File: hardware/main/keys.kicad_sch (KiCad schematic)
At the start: 86 parts, among them SW1 Esc, SW10 a, SW11 \, SW12 Fn, SW13 F2, SW14 2, SW15 w, SW16 s, SW17 z, SW18 Tux, SW19 F3, SW2 F1, SW20 3, SW21 e, SW22 d, SW23 c, SW24 Alt, SW25 F4, SW26 4, SW27 r, SW28 f, SW29 v, SW3 tilde, SW31 F5, SW32 5, SW33 t, SW34 g, SW35 b, SW36 F6, SW37 6, SW38 y, SW39 h, SW4 Tab, SW40 n, SW41 F7, SW42 7, SW43 u, SW44 j, SW45 m, SW46 Space, SW47 F8, SW48 8, SW49 i, SW5 Caps Lock, SW50 k, SW51 ,, SW52 F9, SW53 9, SW54 o, SW55 l, SW56 ., SW57 F10, SW58 0, SW59 p, SW6 Shift, SW60 ;, SW61 /, SW62 Alt Gr, SW63 F11, SW64 -, SW65 [, SW66 ', SW67 Menu, SW68 F12, SW69 =, SW7 Ctrl, SW70 ], SW71 \, SW72 Shift, SW73 Ctrl, SW74 Print, SW75 Backspace, SW76 Enter, SW77 Left, SW78 Scroll Lock, SW79 Up, SW8 1, SW80 Down, SW81 Pause, SW82 INS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

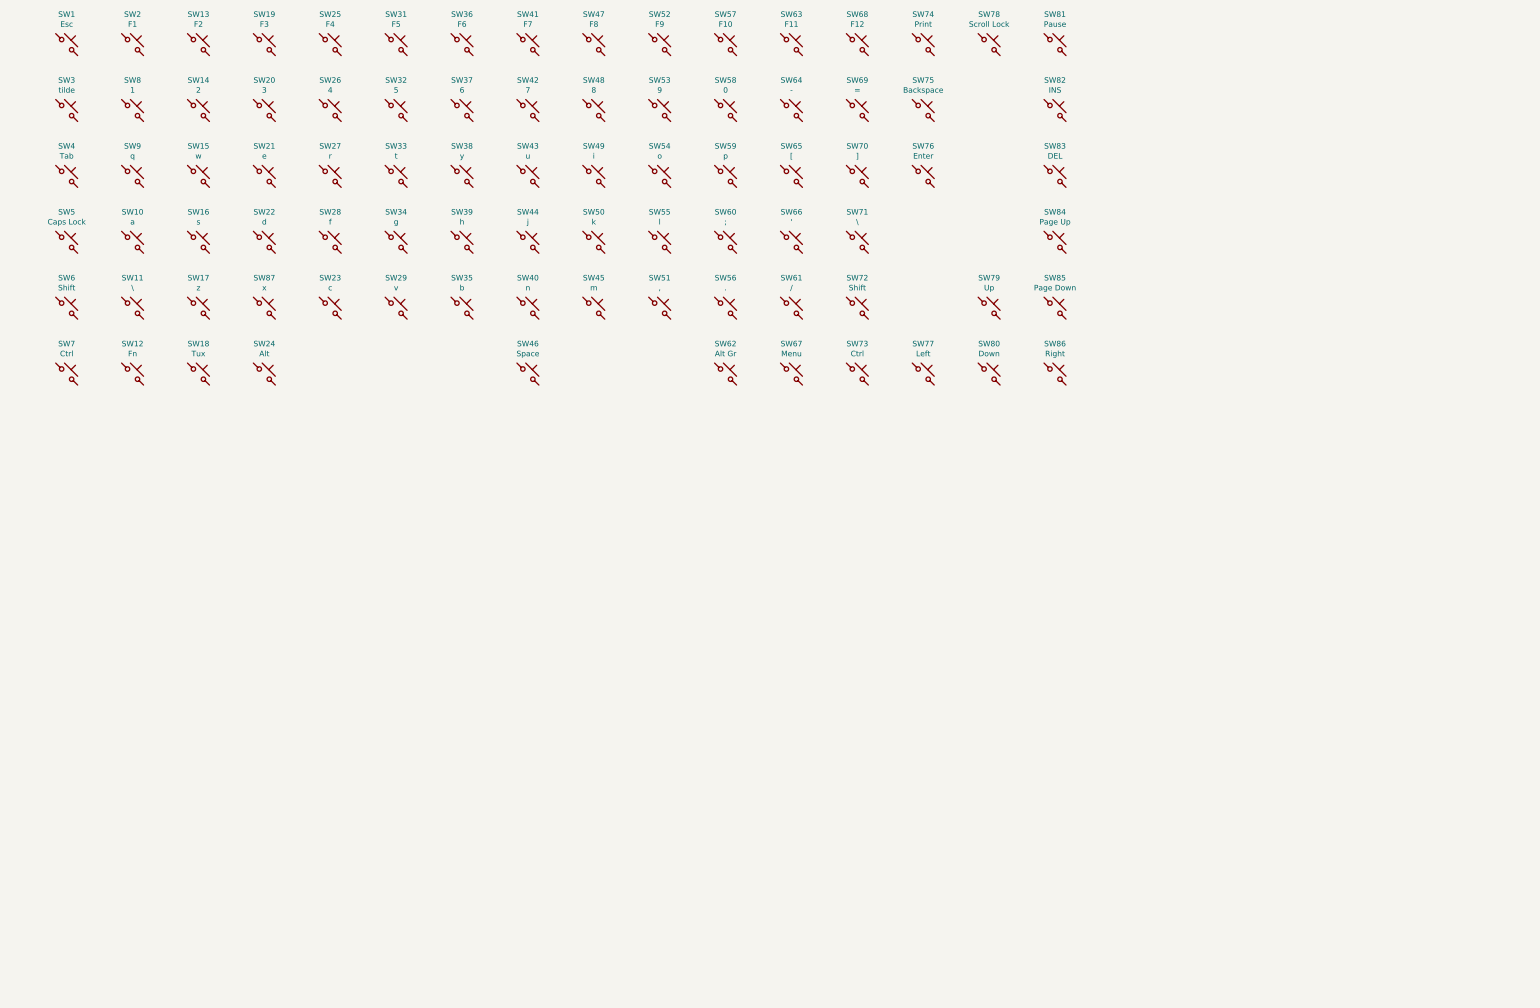
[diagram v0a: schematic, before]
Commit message: Implement the key matrix on the PCB
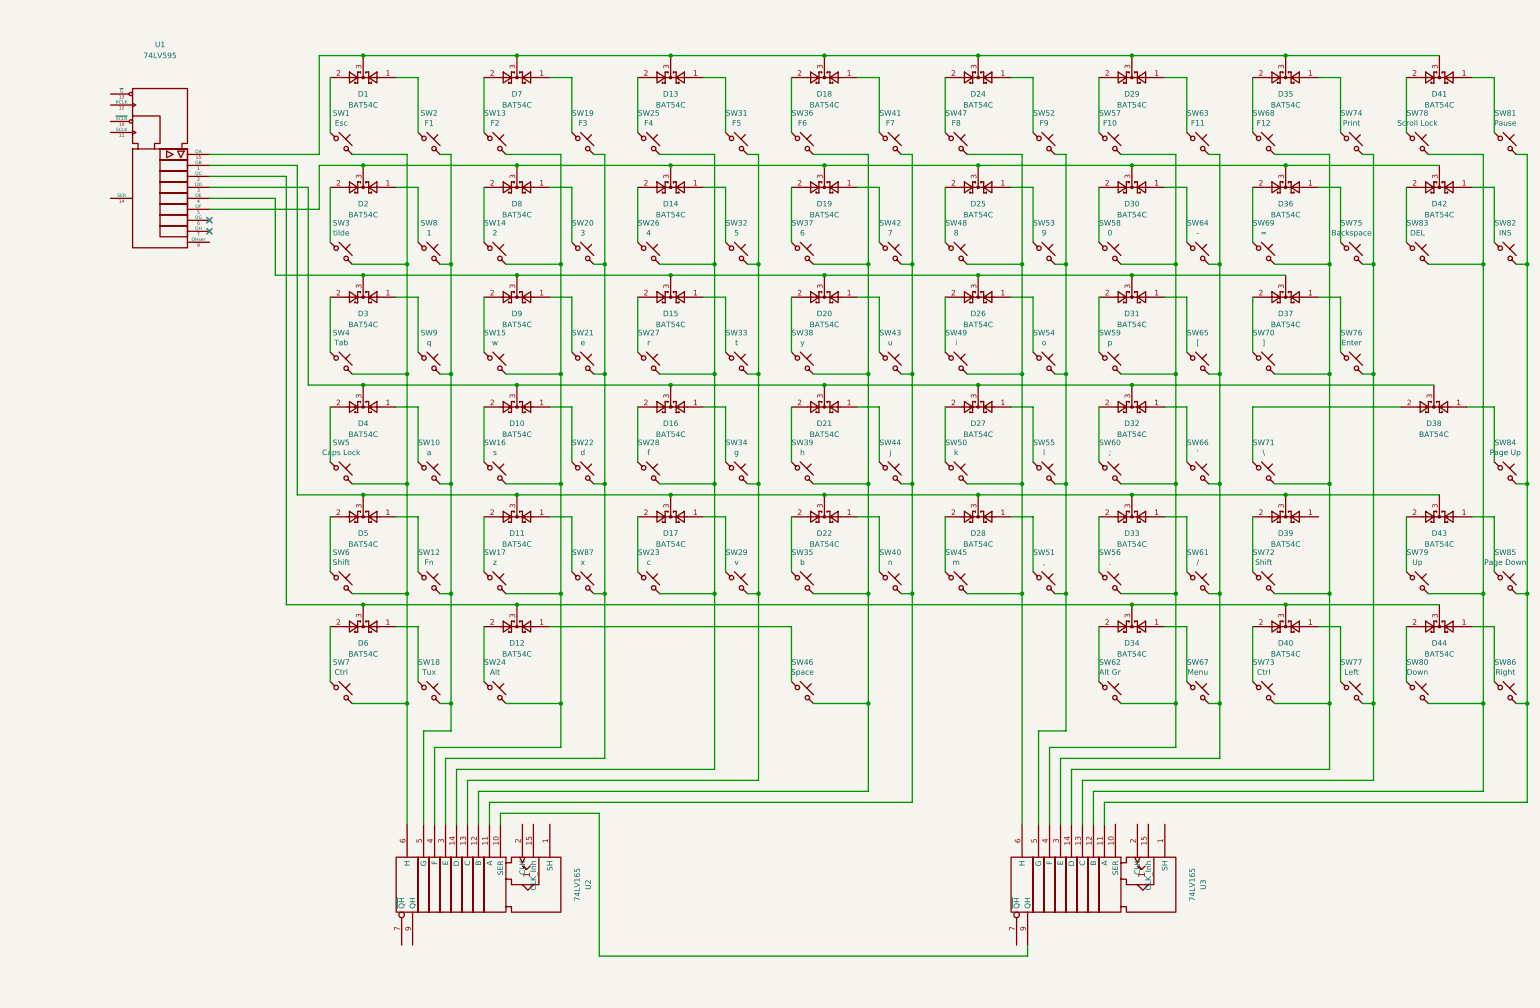
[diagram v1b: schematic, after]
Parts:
- removed SW11: \, footprints:SW_Cherry_MX_1.00u_PCB, symbol Switch:SW_Push_45deg
- added D1, D10, D11, D12, D13, D14, D15, D16, D17, D18, D19, D2, D20, D21, D22, D24, D25, D26, D27, D28, D29, D3, D30, D31, D32, D33, D34, D35, D36, D37, D38, D39, D4, D40, D41, D42, D43, D44, D5, D6, D7, D8, D9: BAT54C, Package_TO_SOT_SMD:SOT-23, symbol Diode:BAT54C
- added U1: 74LV595, Package_SO:TSSOP-16_4.4x5mm_P0.65mm, symbol 74xx_IEEE:74LS595
- added U2, U3: 74LV165, Package_SO:TSSOP-16_4.4x5mm_P0.65mm, symbol 74xx_IEEE:74165
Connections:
- net at SW5.1: now also D4.2
- net at SW5.2: now also SW1.2, SW3.2, SW4.2, SW6.2, SW7.2, U2.6 (H)
- net at SW9.1: now also D3.1
- net at SW9.2: now also SW10.2, SW12.2, SW18.2, SW2.2, SW8.2, U2.5 (G)
- net at SW44.1: now also D21.1
- net at SW44.2: now also SW40.2, SW41.2, SW42.2, SW43.2, U2.11 (A)
- net at SW84.1: now also D38.1
- net at SW84.2: now also SW81.2, SW82.2, SW85.2, SW86.2, U3.11 (A)
- net at SW6.1: now also D5.2
- net at SW65.1: now also D31.1
- net at SW65.2: now also SW61.2, SW63.2, SW64.2, SW66.2, SW67.2, U3.3 (E)
- net at SW56.1: now also D33.2
- net at SW56.2: now also SW57.2, SW58.2, SW59.2, SW60.2, SW62.2, U3.4 (F)
- net at SW78.1: now also D41.2
- net at SW78.2: now also SW79.2, SW80.2, SW83.2, U3.12 (B)
- net at SW73.1: now also D40.2
- net at SW73.2: now also SW68.2, SW69.2, SW70.2, SW71.2, SW72.2, U3.14 (D)
- net at SW7.1: now also D6.2
- net at SW87.1: now also D11.1
- net at SW87.2: now also SW19.2, SW20.2, SW21.2, SW22.2, U2.3 (E)
- net at SW17.1: now also D11.2
- net at SW17.2: now also SW13.2, SW14.2, SW15.2, SW16.2, SW24.2, U2.4 (F)
- net at SW72.1: now also D39.2
- net at SW63.1: now also D29.1
- net at SW50.1: now also D27.2
- net at SW50.2: now also SW45.2, SW47.2, SW48.2, SW49.2, U3.6 (H)
- net at SW8.1: now also D2.1
- net at SW39.1: now also D21.2
- net at SW39.2: now also SW35.2, SW36.2, SW37.2, SW38.2, SW46.2, U2.12 (B)
- net at SW60.1: now also D32.2
- net at SW51.1: now also D28.1
- net at SW51.2: now also SW52.2, SW53.2, SW54.2, SW55.2, U3.5 (G)
- net at SW32.1: now also D14.1
- net at SW32.2: now also SW29.2, SW31.2, SW33.2, SW34.2, U2.13 (C)
- net at SW66.1: now also D32.1
- net at SW20.1: now also D8.1
- net at SW25.1: now also D13.2
- net at SW25.2: now also SW23.2, SW26.2, SW27.2, SW28.2, U2.14 (D)
- net at SW86.1: now also D44.1
- net at SW2.1: now also D1.1
- net at SW81.1: now also D41.1
- net at SW41.1: now also D18.1
- net at SW85.1: now also D43.1
- net at SW27.1: now also D15.2
- net at SW3.1: now also D2.2
- net at SW22.1: now also D10.1
- net at SW48.1: now also D25.2
- net at SW21.1: now also D9.1
- net at SW58.1: now also D30.2
- net at SW37.1: now also D19.2
- net at SW82.1: now also D42.1
- net at SW42.1: now also D19.1
- net at SW53.1: now also D25.1
- net at SW69.1: now also D36.2
- net at SW26.1: now also D14.2
- net at SW16.1: now also D10.2
- net at SW70.1: now also D37.2
- net at SW23.1: now also D17.2
- net at SW57.1: now also D29.2
- net at SW47.1: now also D24.2
- net at SW46.1: now also D12.1
- net at SW80.1: now also D44.2
- net at SW79.1: now also D43.2
- net at SW62.1: now also D34.2
- net at SW64.1: now also D30.1
- net at SW55.1: now also D27.1
- net at SW13.1: now also D7.2
- net at SW35.1: now also D22.2
- net at SW59.1: now also D31.2
- net at SW49.1: now also D26.2
- net at SW54.1: now also D26.1
- net at SW67.1: now also D34.1
- net at SW74.1: now also D35.1
- net at SW74.2: now also SW75.2, SW76.2, SW77.2, U3.13 (C)
- net at SW24.1: now also D12.2
- net at SW1.1: now also D1.2
- net at SW83.1: now also D42.2
- net at SW33.1: now also D15.1
- net at SW77.1: now also D40.1
- net at SW14.1: now also D8.2
- net at SW10.1: now also D4.1
- net at SW18.1: now also D6.1
- net at SW43.1: now also D20.1
- net at SW12.1: now also D5.1
- net at SW4.1: now also D3.2
- net at SW75.1: now also D36.1
- net at SW40.1: now also D22.1
- net at SW15.1: now also D9.2
- net at SW71.1: now also D38.2
- net at SW31.1: now also D13.1
- net at SW19.1: now also D7.1
- net at SW76.1: now also D37.1
- net at SW29.1: now also D17.1
- net at SW36.1: now also D18.2
- net at SW38.1: now also D20.2
- net at SW52.1: now also D24.1
- net at SW45.1: now also D28.2
- net at SW28.1: now also D16.2
- net at SW34.1: now also D16.1
- net at SW68.1: now also D35.2
- net at SW61.1: now also D33.1
- new net: D11.3, D17.3, D22.3, D28.3, D33.3, D39.3, D43.3, D5.3, U1.1 (QB)
- new net: D1.3, D13.3, D18.3, D24.3, D29.3, D35.3, D41.3, D7.3, U1.15 (QA)
- new net: D12.3, D34.3, D40.3, D44.3, D6.3, U1.2 (QC)
- new net: D14.3, D19.3, D2.3, D25.3, D30.3, D36.3, D42.3, D8.3, U1.5 (QF)
- new net: D10.3, D16.3, D21.3, D27.3, D32.3, D38.3, D4.3, U1.3 (QD)
- new net: U2.10 (SER), U3.9 (QH)
- new net: D15.3, D20.3, D26.3, D3.3, D31.3, D37.3, D9.3, U1.4 (QE)
- new net GND: U1.8 (GND), U2.8 (GND), U3.8 (GND)
- new net VCC: U1.16 (VCC), U2.16 (VCC), U3.16 (VCC)
- no-connect marks 0 -> 2
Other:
- moved on the sheet: SW1, SW10, SW12, SW13, SW14, SW15, SW16, SW17, SW18, SW19, SW2, SW20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

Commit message: Add circuit for the shift registers
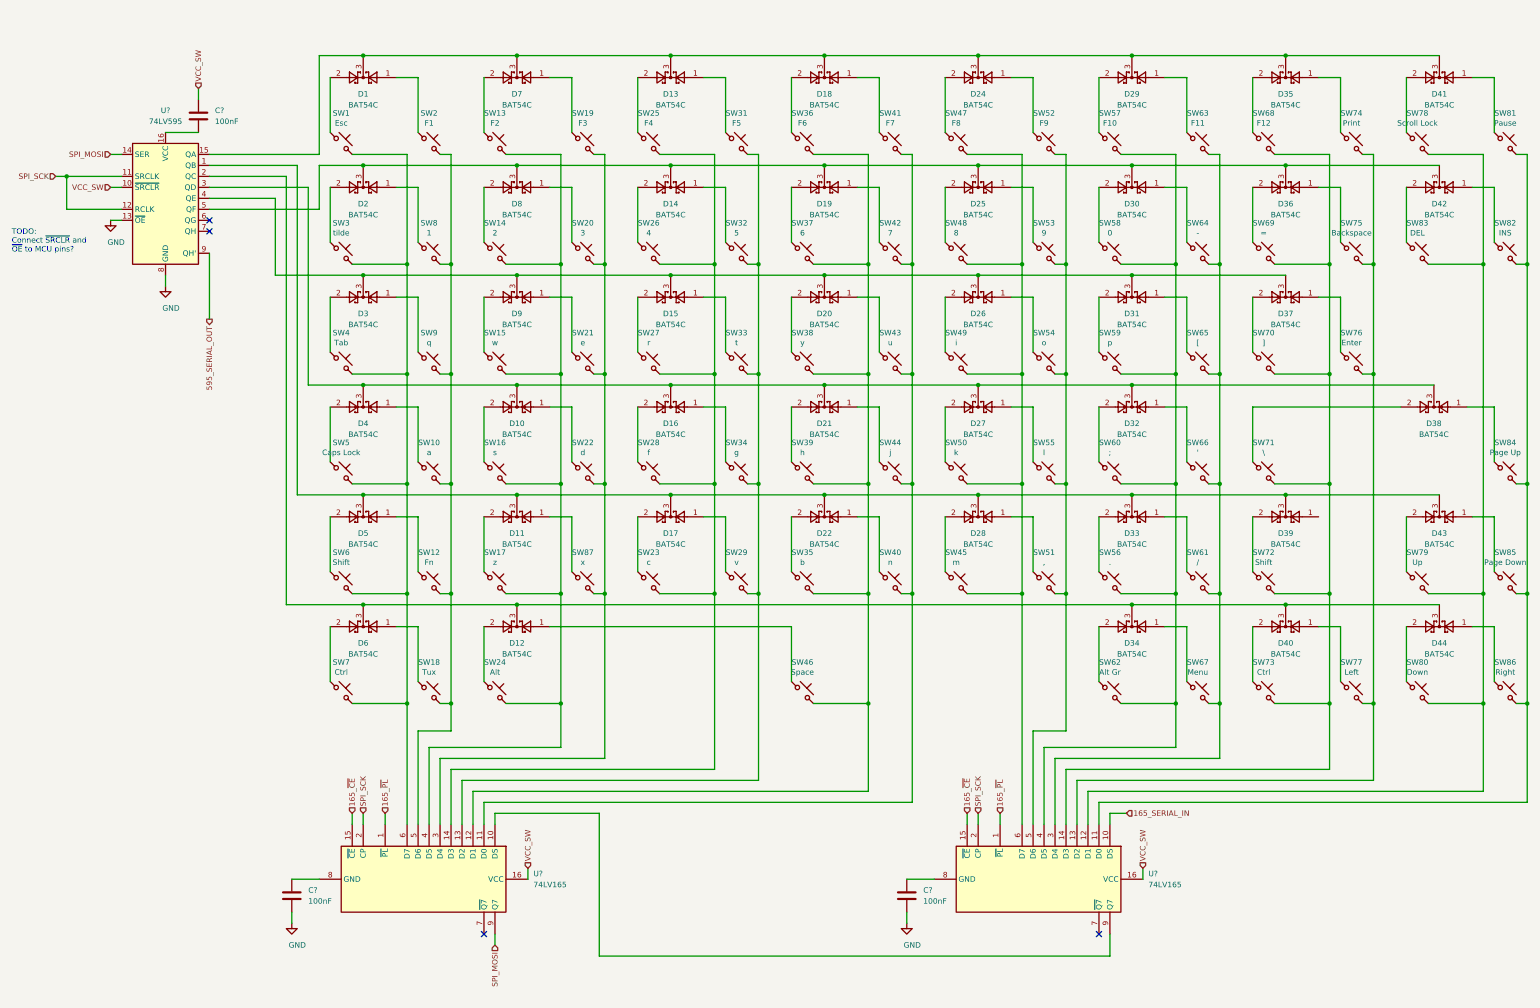
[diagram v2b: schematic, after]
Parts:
- removed U1: 74LV595, Package_SO:TSSOP-16_4.4x5mm_P0.65mm, symbol 74xx_IEEE:74LS595
- removed U2, U3: 74LV165, Package_SO:TSSOP-16_4.4x5mm_P0.65mm, symbol 74xx_IEEE:74165
- added C? (x3): 100nF, symbol Device:C
- added U? (x2): 74LV165, Package_SO:TSSOP-16_4.4x5mm_P0.65mm, symbol 74xx:74LS165
- added U?: 74LV595, Package_SO:TSSOP-16_4.4x5mm_P0.65mm, symbol 74xx:74HC595
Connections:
- net GND: now also C?.2, C?.2, U?.13 (~OE), U?.8 (GND)
- net at SW1.2, SW3.2, SW4.2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: now also U?.6 (D7)
- net at SW10.2, SW12.2, SW18.2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: now also U?.5 (D6)
- net at D11.3, D17.3, D22.3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: now also U?.1 (QB)
- net at D1.3, D13.3, D18.3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: now also U?.15 (QA)
- net at SW40.2, SW41.2, SW42.2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: now also U?.11 (D0)
- net at SW81.2, SW82.2, SW84.2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: now also U?.11 (D0)
- net at D12.3, D34.3, D40.3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: now also U?.2 (QC)
- net at SW61.2, SW63.2, SW64.2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: now also U?.3 (D4)
- net at SW56.2, SW57.2, SW58.2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: now also U?.4 (D5)
- net at SW78.2, SW79.2, SW80.2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: now also U?.12 (D1)
- net at SW68.2, SW69.2, SW70.2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: now also U?.14 (D3)
- net at SW19.2, SW20.2, SW21.2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: now also U?.3 (D4)
- net at SW13.2, SW14.2, SW15.2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: now also U?.4 (D5)
- net at D14.3, D19.3, D2.3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: now also U?.5 (QF)
- net at SW45.2, SW47.2, SW48.2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: now also U?.6 (D7)
- net at SW35.2, SW36.2, SW37.2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: now also U?.12 (D1)
- net at SW51.2, SW52.2, SW53.2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: now also U?.5 (D6)
- net at SW29.2, SW31.2, SW32.2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: now also U?.13 (D2)
- net at SW23.2, SW25.2, SW26.2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: now also U?.14 (D3)
- net at D10.3, D16.3, D21.3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: now also U?.3 (QD)
- net at SW74.2, SW75.2, SW76.2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: now also U?.13 (D2)
- net at D15.3, D20.3, D26.3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: now also U?.4 (QE)
- new net: U?.10 (DS), U?.9 (Q7)
- new net: C?.1, U?.8 (GND) (x2)
- new net: C?.2, U?.16 (VCC)
- new net 165_SERIAL_IN: U?.10 (DS)
- new net 165_~CE: U?.15 (~CE), U?.15 (~CE)
- new net 165_~PL: U?.1 (~PL), U?.1 (~PL)
- new net 595_SERIAL_OUT: U?.9 (QH')
- new net SPI_MOSI: U?.14 (SER), U?.9 (Q7)
- new net SPI_SCK: U?.11 (SRCLK), U?.12 (RCLK), U?.2 (CP), U?.2 (CP)
- new net VCC_SW: C?.1, U?.10 (~SRCLR), U?.16 (VCC), U?.16 (VCC)
- no-connect marks 2 -> 4
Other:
- note added: "TODO: Connect ~SRCLR and ~OE to MCU pins?"

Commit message: Add connector to the numpad to the schematic
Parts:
- U2: renamed from U?; Part Name 74LV595PW -> (none)
- U3: renamed from U?; Part Name 74LV165PW -> (none)
- gave numbers to parts that had none: 4
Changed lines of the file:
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@@
   (junction (at 365.76 154.94) (diameter 1.016) (color 0 0 0 0))
   (junction (at 365.76 180.34) (diameter 1.016) (color 0 0 0 0))
-  (no_connect (at 60.96 71.12))
+  (no_connect (at 60.96 68.58))
   (no_connect (at 124.46 233.68))
   (no_connect (at 266.7 233.68))
-  (no_connect (at 60.96 68.58))
+  (no_connect (at 60.96 71.12))
   (wire (pts (xy 25.4 58.42) (xy 27.94 58.42))
     (stroke (width 0) (type solid) (color 0 0 0 0))
@@
   (symbol (lib_id "power:GND") (at 38.1 68.58 0) (unit 1)
     (in_bom yes) (on_board yes)
-    (property "Reference" "#PWR?" (id 0) (at 38.1 74.93 0)
+    (property "Reference" "#PWR0111" (id 0) (at 38.1 74.93 0)
       (effects (font (size 1.27 1.27)) hide)
     )
@@
   (symbol (lib_id "power:GND") (at 50.8 83.82 0) (unit 1)
     (in_bom yes) (on_board yes)
-    (property "Reference" "#PWR?" (id 0) (at 50.8 90.17 0)
+    (property "Reference" "#PWR0112" (id 0) (at 50.8 90.17 0)
       (effects (font (size 1.27 1.27)) hide)
     )
@@
   (symbol (lib_id "power:GND") (at 80.01 231.14 0) (unit 1)
     (in_bom yes) (on_board yes)
-    (property "Reference" "#PWR?" (id 0) (at 80.01 237.49 0)
+    (property "Reference" "#PWR0113" (id 0) (at 80.01 237.49 0)
       (effects (font (size 1.27 1.27)) hide)
     )
@@
   (symbol (lib_id "power:GND") (at 222.25 231.14 0) (unit 1)
     (in_bom yes) (on_board yes)
-    (property "Reference" "#PWR?" (id 0) (at 222.25 237.49 0)
+    (property "Reference" "#PWR0110" (id 0) (at 222.25 237.49 0)
       (effects (font (size 1.27 1.27)) hide)
     )
@@
   (symbol (lib_id "Device:C") (at 58.42 44.45 0) (unit 1)
     (in_bom yes) (on_board yes)
-    (property "Reference" "C?" (id 0) (at 62.23 43.18 0)
+    (property "Reference" "C4" (id 0) (at 62.23 43.18 0)
       (effects (font (size 1.27 1.27)) (justify left))
     )
@@
   (symbol (lib_id "Device:C") (at 80.01 224.79 0) (unit 1)
     (in_bom yes) (on_board yes)
-    (property "Reference" "C?" (id 0) (at 83.82 223.52 0)
+    (property "Reference" "C5" (id 0) (at 83.82 223.52 0)
       (effects (font (size 1.27 1.27)) (justify left))
     )
@@
   (symbol (lib_id "Device:C") (at 222.25 224.79 0) (unit 1)
     (in_bom yes) (on_board yes)
-    (property "Reference" "C?" (id 0) (at 226.06 223.52 0)
+    (property "Reference" "C6" (id 0) (at 226.06 223.52 0)
       (effects (font (size 1.27 1.27)) (justify left))
     )
@@
   (symbol (lib_id "74xx:74HC595") (at 50.8 63.5 0) (unit 1)
     (in_bom yes) (on_board yes)
-    (property "Reference" "U?" (id 0) (at 50.8 43.18 0))
+    (property "Reference" "U2" (id 0) (at 50.8 43.18 0))
     (property "Value" "74LV595" (id 1) (at 50.8 45.72 0))
     (property "Footprint" "Package_SO:TSSOP-16_4.4x5mm_P0.65mm" (id 2) (at 50.8 63.5 0)
@@
       (effects (font (size 1.27 1.27)) hide)
     )
-    (property "Part Name" "74LV595PW" (id 5) (at 50.8 63.5 0)
-      (effects (font (size 1.27 1.27)) hide)
-    )
     (property "Mouser" " 771-74LV595PW-T" (id 4) (at 50.8 63.5 0)
       (effects (font (size 1.27 1.27)) hide)
@@
   (symbol (lib_id "74xx:74LS165") (at 111.76 220.98 270) (unit 1)
     (in_bom yes) (on_board yes)
-    (property "Reference" "U?" (id 0) (at 135.89 219.71 90)
+    (property "Reference" "U3" (id 0) (at 135.89 219.71 90)
       (effects (font (size 1.27 1.27)) (justify left))
     )
@@
       (effects (font (size 1.27 1.27)) hide)
     )
-    (property "Part Name" "74LV165PW" (id 5) (at 111.76 220.98 90)
-      (effects (font (size 1.27 1.27)) hide)
-    )
     (property "Mouser" " 771-LV165PW112 " (id 4) (at 111.76 220.98 90)
       (effects (font (size 1.27 1.27)) hide)
@@
   (symbol (lib_id "74xx:74LS165") (at 254 220.98 270) (unit 1)
     (in_bom yes) (on_board yes)
-    (property "Reference" "U?" (id 0) (at 278.13 219.71 90)
+    (property "Reference" "U4" (id 0) (at 278.13 219.71 90)
       (effects (font (size 1.27 1.27)) (justify left))
     )

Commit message: Modify the connection to the numpad
As the numpad now uses a stm-microcontroller instead of the
shift-registers the connection is changed to UART.
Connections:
- net 165_SERIAL_IN: no longer names the net of U4.10 (DS)
- net 595_SERIAL_OUT: no longer names the net of U2.9 (QH')
- no-connect marks 4 -> 6
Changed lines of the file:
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@@
   (junction (at 365.76 180.34) (diameter 1.016) (color 0 0 0 0))
   (no_connect (at 60.96 68.58))
+  (no_connect (at 266.7 233.68))
   (no_connect (at 124.46 233.68))
-  (no_connect (at 266.7 233.68))
   (no_connect (at 60.96 71.12))
+  (no_connect (at 60.96 76.2))
+  (no_connect (at 269.24 208.28))
   (wire (pts (xy 25.4 58.42) (xy 27.94 58.42))
     (stroke (width 0) (type solid) (color 0 0 0 0))
@@
     (stroke (width 0) (type solid) (color 0 0 0 0))
   )
-  (wire (pts (xy 60.96 76.2) (xy 60.96 91.44))
-    (stroke (width 0) (type solid) (color 0 0 0 0))
-  )
   (wire (pts (xy 76.2 81.28) (xy 76.2 63.5))
     (stroke (width 0) (type solid) (color 0 0 0 0))
@@
   )
   (wire (pts (xy 266.7 208.28) (xy 266.7 203.2))
-    (stroke (width 0) (type solid) (color 0 0 0 0))
-  )
-  (wire (pts (xy 269.24 205.74) (xy 273.05 205.74))
-    (stroke (width 0) (type solid) (color 0 0 0 0))
-  )
-  (wire (pts (xy 269.24 208.28) (xy 269.24 205.74))
     (stroke (width 0) (type solid) (color 0 0 0 0))
   )
@@
     (effects (font (size 1.27 1.27)) (justify left))
   )
-  (hierarchical_label "595_SERIAL_OUT" (shape output) (at 60.96 91.44 270)
-    (effects (font (size 1.27 1.27)) (justify right))
-  )
   (hierarchical_label "165_~CE" (shape input) (at 93.98 205.74 90)
     (effects (font (size 1.27 1.27)) (justify left))
@@
     (effects (font (size 1.27 1.27)) (justify left))
   )
-  (hierarchical_label "165_SERIAL_IN" (shape input) (at 273.05 205.74 0)
-    (effects (font (size 1.27 1.27)) (justify left))
-  )
